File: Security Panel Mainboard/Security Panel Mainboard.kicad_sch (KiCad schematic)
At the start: 66 parts, among them IC1 LM358DT, J1 CTB0508_3, J2 CTB0508_3, J3 CTB0508_3, J4 CTB0508_3, J5 CTB0508_3, J6 CTB0508_3, J7 CTB0508_5, J8 CTB0708/2, J9 SPI Programming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

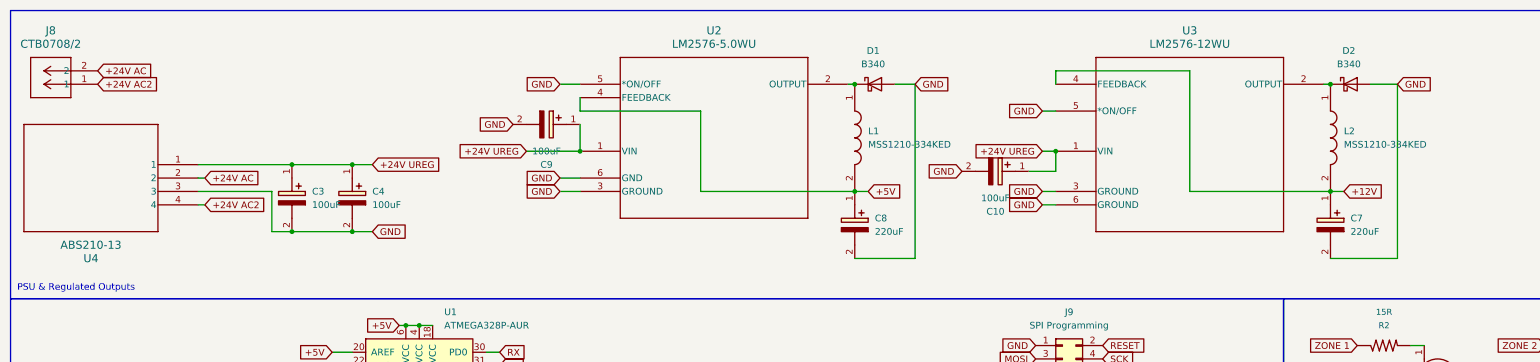
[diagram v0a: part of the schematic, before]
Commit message: Design Changes to PSU and Mainboard
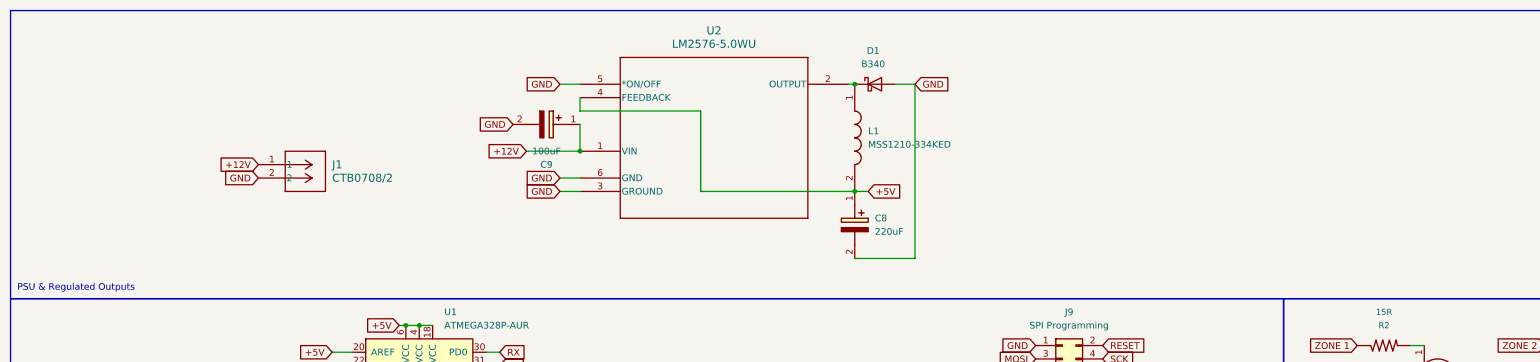
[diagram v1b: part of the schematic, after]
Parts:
- removed C10, C3, C4: 100uF, SamacSys_Parts:CAPAE1050X1250N, symbol SamacSys_Parts:MAL214699104E3
- removed C7: 220uF, SamacSys_Parts:EEE0JA152UAP, symbol SamacSys_Parts:EEEFK1H221P
- removed D2: B340, Diode_SMD:D_SMC, symbol Diode:B340
- removed J8: CTB0708/2, CTB0708-2:CONN-2X1_CTB0708&slash_2_CMD, symbol CTB0708-2:CTB0708_2
- removed L2: MSS1210-334KED, SamacSys_Parts:INDPM123123X1020N, symbol SamacSys_Parts:MSS1210-334KED
- removed U3: LM2576-12WU, LM2576-12WU:TO-263-5_U_MCH, symbol LM2576-12WU:LM2576-12WU
- removed U4: ABS210-13, ABS210-13:SON_S210-13_DIO, symbol ABS210-13:ABS210-13
- added J1: CTB0708/2, CTB0708-2:CONN-2X1_CTB0708&slash_2_CMD, symbol CTB0708-2:CTB0708_2
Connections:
- net +24V UREG is gone; now on net +12V: C9.1 (+), U2.1 (VIN)
- net +12V: now also J1.1
- net GND: now also J1.2
